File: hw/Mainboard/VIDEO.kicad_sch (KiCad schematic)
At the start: 1 part, among them J9 PET_Video

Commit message: hw: wip
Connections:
- net GND renamed PD_GND
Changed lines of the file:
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@@
     (stroke (width 0) (type default) (color 0 0 0 0))
   )
-  (wire (pts (xy 146.05 77.47) (xy 146.05 80.01))
+  (wire (pts (xy 146.05 77.47) (xy 146.05 78.74))
     (stroke (width 0) (type default) (color 0 0 0 0))
   )
@@
     (effects (font (size 1.27 1.27)) (justify right))
   )
-  (symbol (lib_id "power:GND") (at 146.05 80.01 0) (unit 1)
+  (symbol (lib_id "PET:PD_GND") (at 146.05 78.74 0) (unit 1)
     (in_bom yes) (on_board yes) (fields_autoplaced)
-    (property "Reference" "#PWR0141" (id 0) (at 146.05 86.36 0)
+    (property "Reference" "#PWR0176" (id 0) (at 146.05 85.09 0)
       (effects (font (size 1.27 1.27)) hide)
     )
-    (property "Value" "GND" (id 1) (at 146.05 85.09 0))
-    (property "Footprint" "" (id 2) (at 146.05 80.01 0)
+    (property "Value" "PD_GND" (id 1) (at 146.05 83.82 0))
+    (property "Footprint" "" (id 2) (at 146.05 78.74 0)
       (effects (font (size 1.27 1.27)) hide)
     )
-    (property "Datasheet" "" (id 3) (at 146.05 80.01 0)
+    (property "Datasheet" "" (id 3) (at 146.05 78.74 0)
       (effects (font (size 1.27 1.27)) hide)
     )

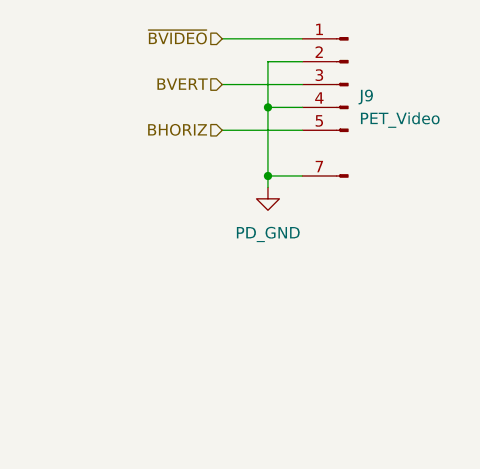
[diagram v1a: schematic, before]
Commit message: hw: larger schematic pages, routed w/netties
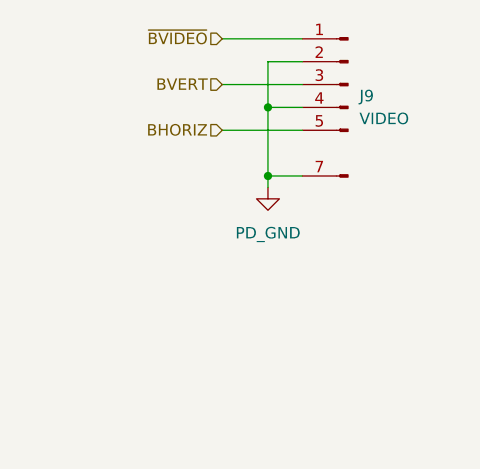
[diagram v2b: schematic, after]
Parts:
- J9: value PET_Video -> VIDEO; symbol PET:PET_Video -> Retrocomputing:CBM_PET_VIDEO_Conn_Keyed
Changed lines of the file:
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@@
 (kicad_sch (version 20211123) (generator eeschema)
-  (paper "A4")
+  (paper "B")
   (junction (at 146.05 69.85) (diameter 0) (color 0 0 0 0)
   )
@@
     (pin "1")
   )
-  (symbol (lib_id "PET:PET_Video") (at 154.94 69.85 0) (mirror y) (unit 1)
+  (symbol (lib_id "Retrocomputing:CBM_PET_VIDEO_Conn_Keyed") (at 154.94 69.85 0) (mirror y) (unit 1)
     (in_bom yes) (on_board yes) (fields_autoplaced)
     (property "Reference" "J9" (id 0) (at 156.21 68.5799 0)
       (effects (font (size 1.27 1.27)) (justify right))
     )
-    (property "Value" "PET_Video" (id 1) (at 156.21 71.1199 0)
+    (property "Value" "VIDEO" (id 1) (at 156.21 71.1199 0)
       (effects (font (size 1.27 1.27)) (justify right))
     )

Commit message: hw: tidy power and resize pages
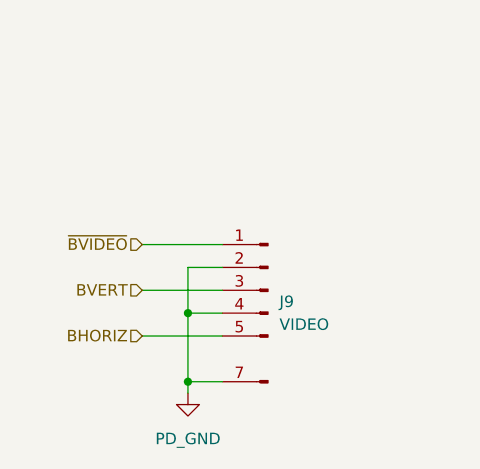
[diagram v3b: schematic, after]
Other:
- title: (none) -> CBM PET Mainboard Replacement
- moved on the sheet: J9
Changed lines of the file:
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@@
 (kicad_sch (version 20211123) (generator eeschema)
-  (paper "B")
-  (junction (at 146.05 69.85) (diameter 0) (color 0 0 0 0)
+  (paper "A")
+  (title_block
+    (title "CBM PET Mainboard Replacement")
   )
-  (junction (at 146.05 77.47) (diameter 0) (color 0 0 0 0)
+  (junction (at 137.16 92.71) (diameter 0) (color 0 0 0 0)
   )
-  (wire (pts (xy 146.05 69.85) (xy 146.05 77.47))
+  (junction (at 137.16 100.33) (diameter 0) (color 0 0 0 0)
+  )
+  (wire (pts (xy 137.16 92.71) (xy 137.16 100.33))
     (stroke (width 0) (type default) (color 0 0 0 0))
   )
-  (wire (pts (xy 146.05 69.85) (xy 149.86 69.85))
+  (wire (pts (xy 137.16 92.71) (xy 140.97 92.71))
     (stroke (width 0) (type default) (color 0 0 0 0))
   )
-  (wire (pts (xy 146.05 64.77) (xy 146.05 69.85))
+  (wire (pts (xy 137.16 87.63) (xy 137.16 92.71))
     (stroke (width 0) (type default) (color 0 0 0 0))
   )
-  (wire (pts (xy 146.05 77.47) (xy 149.86 77.47))
+  (wire (pts (xy 137.16 100.33) (xy 140.97 100.33))
     (stroke (width 0) (type default) (color 0 0 0 0))
   )
-  (wire (pts (xy 140.97 72.39) (xy 149.86 72.39))
+  (wire (pts (xy 132.08 95.25) (xy 140.97 95.25))
     (stroke (width 0) (type default) (color 0 0 0 0))
   )
-  (wire (pts (xy 140.97 62.23) (xy 149.86 62.23))
+  (wire (pts (xy 132.08 85.09) (xy 140.97 85.09))
     (stroke (width 0) (type default) (color 0 0 0 0))
   )
-  (wire (pts (xy 149.86 64.77) (xy 146.05 64.77))
+  (wire (pts (xy 140.97 87.63) (xy 137.16 87.63))
     (stroke (width 0) (type default) (color 0 0 0 0))
   )
-  (wire (pts (xy 140.97 67.31) (xy 149.86 67.31))
+  (wire (pts (xy 132.08 90.17) (xy 140.97 90.17))
     (stroke (width 0) (type default) (color 0 0 0 0))
   )
-  (wire (pts (xy 146.05 77.47) (xy 146.05 78.74))
+  (wire (pts (xy 137.16 100.33) (xy 137.16 101.6))
     (stroke (width 0) (type default) (color 0 0 0 0))
   )
-  (hierarchical_label "BHORIZ" (shape input) (at 140.97 72.39 180)
+  (hierarchical_label "BHORIZ" (shape input) (at 132.08 95.25 180)
     (effects (font (size 1.27 1.27)) (justify right))
   )
-  (hierarchical_label "~{BVIDEO}" (shape input) (at 140.97 62.23 180)
+  (hierarchical_label "~{BVIDEO}" (shape input) (at 132.08 85.09 180)
     (effects (font (size 1.27 1.27)) (justify right))
   )
-  (hierarchical_label "BVERT" (shape input) (at 140.97 67.31 180)
+  (hierarchical_label "BVERT" (shape input) (at 132.08 90.17 180)
     (effects (font (size 1.27 1.27)) (justify right))
   )
-  (symbol (lib_id "PET:PD_GND") (at 146.05 78.74 0) (unit 1)
+  (symbol (lib_id "PET:PD_GND") (at 137.16 101.6 0) (unit 1)
     (in_bom yes) (on_board yes) (fields_autoplaced)
-    (property "Reference" "#PWR0176" (id 0) (at 146.05 85.09 0)
+    (property "Reference" "#PWR0176" (id 0) (at 137.16 107.95 0)
       (effects (font (size 1.27 1.27)) hide)
     )
-    (property "Value" "PD_GND" (id 1) (at 146.05 83.82 0))
-    (property "Footprint" "" (id 2) (at 146.05 78.74 0)
+    (property "Value" "PD_GND" (id 1) (at 137.16 106.68 0))
+    (property "Footprint" "" (id 2) (at 137.16 101.6 0)
       (effects (font (size 1.27 1.27)) hide)
     )
-    (property "Datasheet" "" (id 3) (at 146.05 78.74 0)
+    (property "Datasheet" "" (id 3) (at 137.16 101.6 0)
       (effects (font (size 1.27 1.27)) hide)
     )
     (pin "1")
   )
-  (symbol (lib_id "Retrocomputing:CBM_PET_VIDEO_Conn_Keyed") (at 154.94 69.85 0) (mirror y) (unit 1)
+  (symbol (lib_id "Retrocomputing:CBM_PET_VIDEO_Conn_Keyed") (at 146.05 92.71 0) (mirror y) (unit 1)
     (in_bom yes) (on_board yes) (fields_autoplaced)
-    (property "Reference" "J9" (id 0) (at 156.21 68.5799 0)
+    (property "Reference" "J9" (id 0) (at 147.32 91.4399 0)
       (effects (font (size 1.27 1.27)) (justify right))
     )
-    (property "Value" "VIDEO" (id 1) (at 156.21 71.1199 0)
+    (property "Value" "VIDEO" (id 1) (at 147.32 93.9799 0)
       (effects (font (size 1.27 1.27)) (justify right))
     )
-    (property "Footprint" "PET:PET_Video" (id 2) (at 154.94 69.85 0)
+    (property "Footprint" "PET:PET_Video" (id 2) (at 146.05 92.71 0)
       (effects (font (size 1.27 1.27)) hide)
     )
-    (property "Datasheet" "~" (id 3) (at 154.94 69.85 0)
+    (property "Datasheet" "~" (id 3) (at 146.05 92.71 0)
       (effects (font (size 1.27 1.27)) hide)
     )

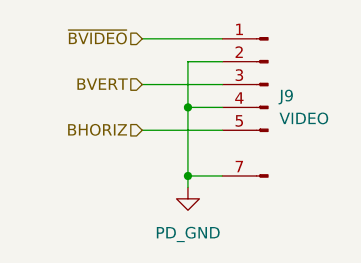
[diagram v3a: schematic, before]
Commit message: hw: remove bar from video signal name
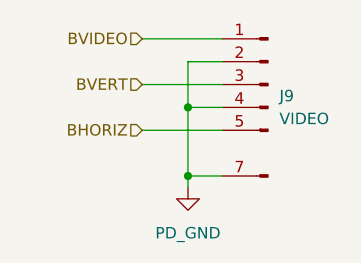
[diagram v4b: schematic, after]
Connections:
- net ~{BVIDEO} renamed BVIDEO
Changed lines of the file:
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@@
     (effects (font (size 1.27 1.27)) (justify right))
   )
-  (hierarchical_label "~{BVIDEO}" (shape input) (at 132.08 85.09 180)
+  (hierarchical_label "BVIDEO" (shape input) (at 132.08 85.09 180)
     (effects (font (size 1.27 1.27)) (justify right))
   )

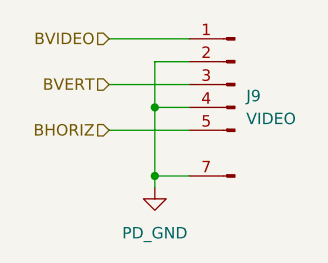
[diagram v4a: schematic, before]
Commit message: hw: tidy MCU and a few missed PD_
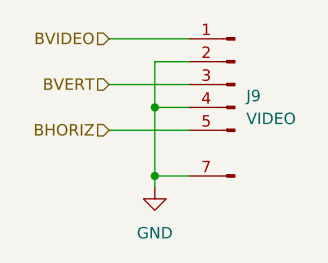
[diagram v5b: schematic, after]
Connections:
- net PD_GND renamed GND
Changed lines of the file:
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@@
     (effects (font (size 1.27 1.27)) (justify right))
   )
-  (symbol (lib_id "PET:PD_GND") (at 137.16 101.6 0) (unit 1)
+  (symbol (lib_id "power:GND") (at 137.16 101.6 0) (unit 1)
     (in_bom yes) (on_board yes) (fields_autoplaced)
-    (property "Reference" "#PWR0176" (id 0) (at 137.16 107.95 0)
+    (property "Reference" "#PWR?" (id 0) (at 137.16 107.95 0)
       (effects (font (size 1.27 1.27)) hide)
     )
-    (property "Value" "PD_GND" (id 1) (at 137.16 106.68 0))
+    (property "Value" "GND" (id 1) (at 137.16 106.68 0))
     (property "Footprint" "" (id 2) (at 137.16 101.6 0)
       (effects (font (size 1.27 1.27)) hide)

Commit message: hw: wip
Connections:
- net GND renamed PD_GND
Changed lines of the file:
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@@
     (effects (font (size 1.27 1.27)) (justify right))
   )
-  (symbol (lib_id "power:GND") (at 137.16 101.6 0) (unit 1)
+  (symbol (lib_id "PET:PD_GND") (at 137.16 101.6 0) (unit 1)
     (in_bom yes) (on_board yes) (fields_autoplaced)
-    (property "Reference" "#PWR0139" (id 0) (at 137.16 107.95 0)
+    (property "Reference" "#PWR0163" (id 0) (at 137.16 107.95 0)
       (effects (font (size 1.27 1.27)) hide)
     )
-    (property "Value" "GND" (id 1) (at 137.16 106.68 0))
+    (property "Value" "PD_GND" (id 1) (at 137.16 106.68 0))
     (property "Footprint" "" (id 2) (at 137.16 101.6 0)
       (effects (font (size 1.27 1.27)) hide)

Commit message: hw: add more Mouse part numbers
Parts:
- J9: MOUSER (none) -> 649-1012937893603BLF
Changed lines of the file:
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@@
+      (effects (font (size 1.27 1.27)) hide)
+    )
+    (property "MOUSER" "649-1012937893603BLF" (id 4) (at 146.05 92.71 0)
       (effects (font (size 1.27 1.27)) hide)
     )
